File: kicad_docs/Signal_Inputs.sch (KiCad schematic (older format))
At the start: 16 parts, among them J1 tuning controls, J2 1 v/oct inputs, J3 linear FM input, J4 sync input, J5 PWM inputs

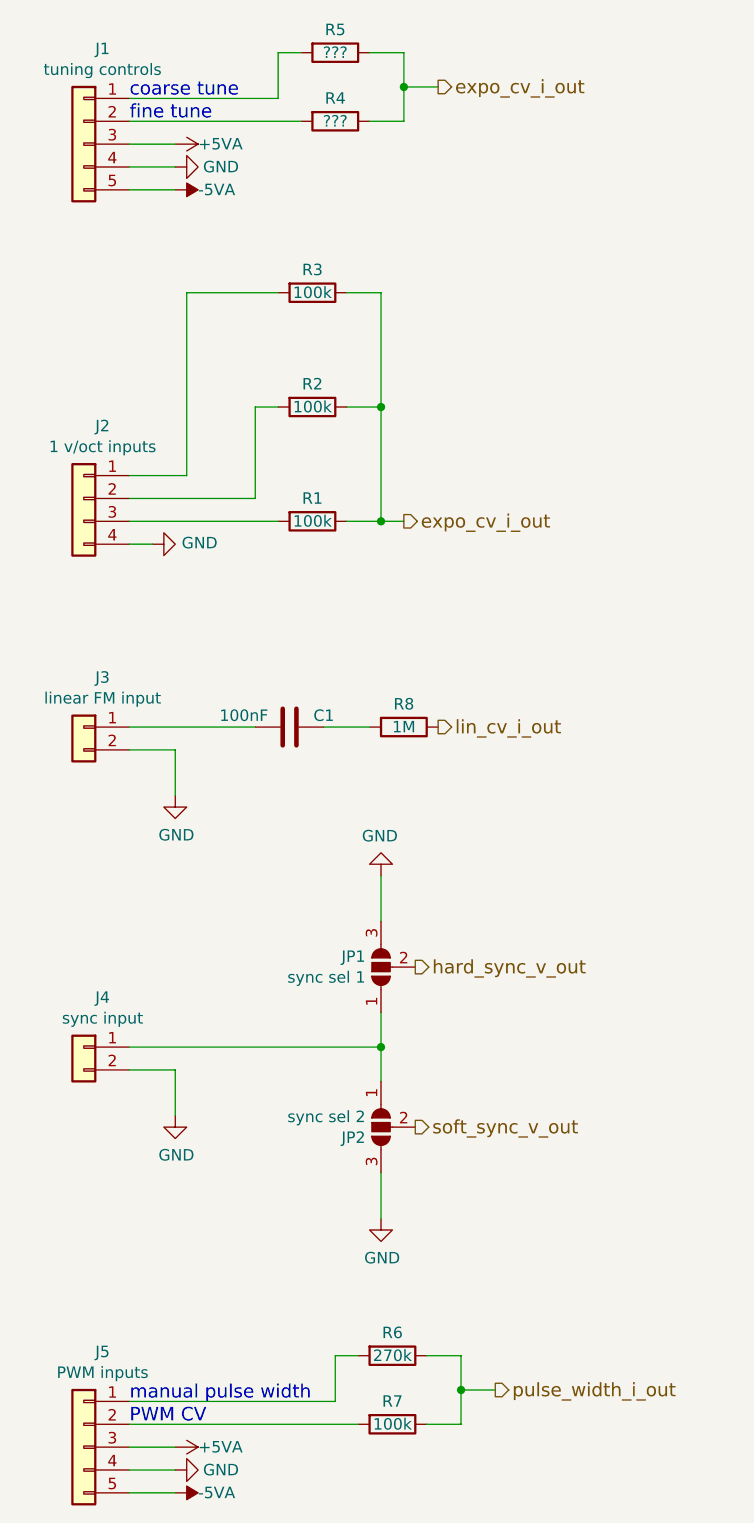
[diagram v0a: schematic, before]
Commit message: update and fill in some resistor values
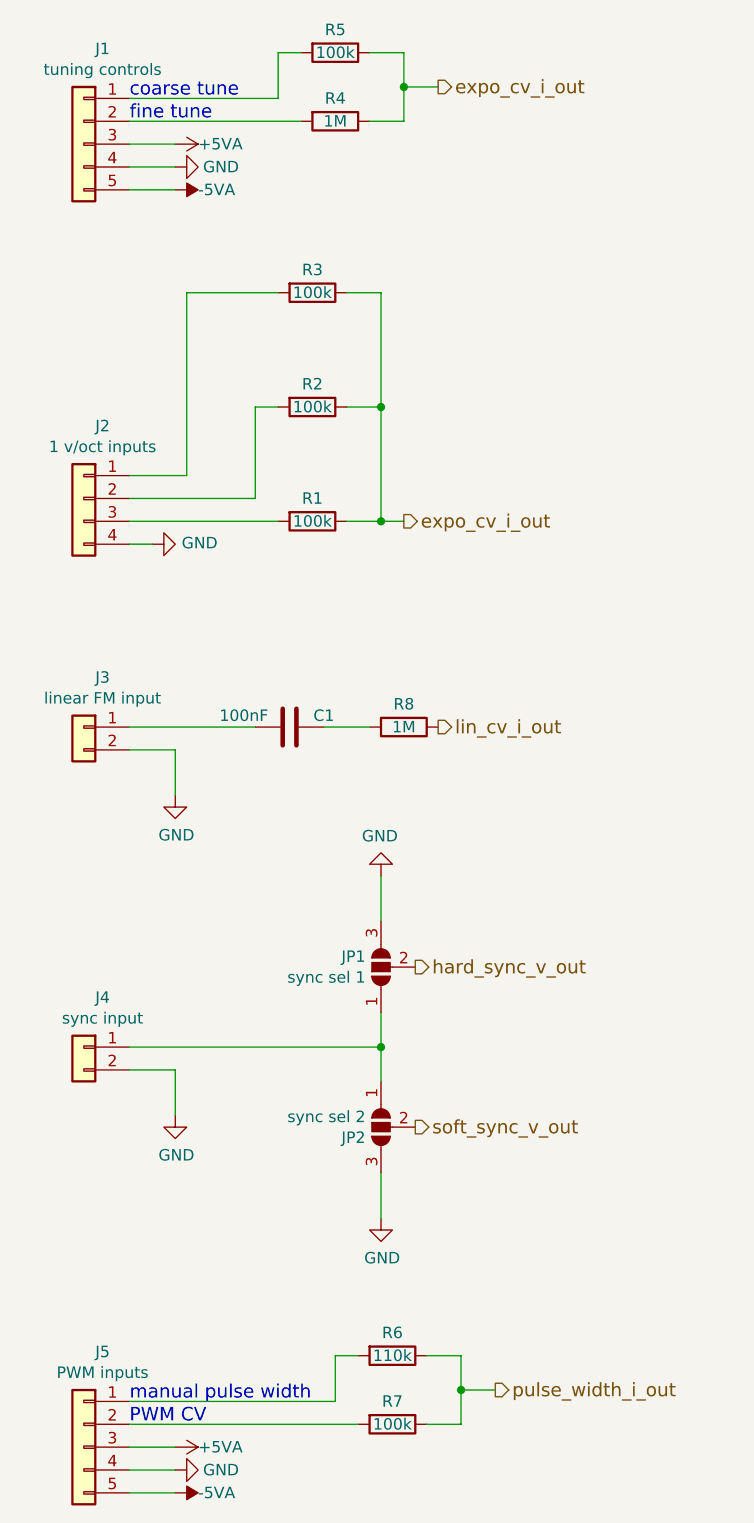
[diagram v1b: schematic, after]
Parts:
- R4: value ??? -> 1M
- R5: value ??? -> 100k
- R6: value 270k -> 110k
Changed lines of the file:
@@
 encoding utf-8
 Sheet 2 4
-Title ""
+Title "CEM3340 VCO Signal Inputs"
 Date "2020-01-30"
 Rev "1"
@@
 AR Path="/5E3EE0AD/5E9947EB" Ref="R5"  Part="1"
 F 0 "R5" V 4100 1000 50  0000 C CNN
-F 1 "???" V 4200 1000 50  0000 C CNN
+F 1 "100k" V 4200 1000 50  0000 C CNN
 F 2 "Resistor_SMD:R_0805_2012Metric_Pad1.15x1.40mm_HandSolder" V 4130 1000 50  0001 C CNN
 F 3 "~" H 4200 1000 50  0001 C CNN
@@
 AR Path="/5E3EE0AD/5E994813" Ref="R6"  Part="1"
 F 0 "R6" V 4350 6700 50  0000 C CNN
-F 1 "270k" V 4450 6700 50  0000 C CNN
+F 1 "110k" V 4450 6700 50  0000 C CNN
 F 2 "Resistor_SMD:R_0805_2012Metric_Pad1.15x1.40mm_HandSolder" V 4380 6700 50  0001 C CNN
 F 3 "~" H 4450 6700 50  0001 C CNN
@@
 AR Path="/5E3EE0AD/5E994832" Ref="R4"  Part="1"
 F 0 "R4" V 4100 1300 50  0000 C CNN
-F 1 "???" V 4200 1300 50  0000 C CNN
+F 1 "1M" V 4200 1300 50  0000 C CNN
 F 2 "Resistor_SMD:R_0805_2012Metric_Pad1.15x1.40mm_HandSolder" V 4130 1300 50  0001 C CNN
 F 3 "~" H 4200 1300 50  0001 C CNN
